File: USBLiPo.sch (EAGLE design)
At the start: 11 parts, among them IC1 LTC4054, J1 Battery, J2 USB, Q1 2N7002

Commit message: fixed charge current program
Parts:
- Q1: device freetronics-master-v1:MOSFET-NCHANNELSMD -> freetronics-luke:2N7002
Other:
- moved on the sheet: Q1
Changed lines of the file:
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@@
 <part name="IC1" library="freetronics-luke" deviceset="LTC4054" device=""/>
 <part name="U$1" library="freetronics-luke" deviceset="GND" device=""/>
-<part name="Q1" library="freetronics-master-v1" deviceset="MOSFET-NCHANNEL" device="SMD" value="2N7002"/>
 <part name="R1" library="freetronics" deviceset="RESISTOR" device="0603" value="1k"/>
 <part name="R2" library="freetronics" deviceset="RESISTOR" device="0603" value="10k"/>
@@
 <part name="LED2" library="freetronics-master-v1" deviceset="LED" device="0603" value="Red"/>
 <part name="J2" library="freetronics-luke" deviceset="USB-FT" device="" value="USB"/>
+<part name="Q1" library="freetronics-luke" deviceset="2N7002" device=""/>
 </parts>
 <sheets>
@@
 </instance>
 <instance part="U$1" gate="G$1" x="86.36" y="53.34"/>
-<instance part="Q1" gate="G$1" x="132.08" y="68.58" smashed="yes">
-<attribute name="NAME" x="119.38" y="73.66" size="1.27" layer="95"/>
-<attribute name="VALUE" x="119.38" y="71.12" size="1.27" layer="96"/>
-</instance>
 <instance part="R1" gate="G$1" x="109.22" y="91.44" smashed="yes" rot="MR180">
 <attribute name="NAME" x="106.68" y="96.52" size="1.27" layer="95"/>
@@
 </instance>
 <instance part="J2" gate="G$1" x="35.56" y="71.12"/>
+<instance part="Q1" gate="G$1" x="132.08" y="68.58" smashed="yes">
+<attribute name="NAME" x="119.38" y="73.66" size="1.27" layer="95"/>
+<attribute name="VALUE" x="119.38" y="71.12" size="1.27" layer="96"/>
+</instance>
 </instances>
 <busses>
@@
 <segment>
 <wire x1="132.08" y1="63.5" x2="132.08" y2="55.88" width="0.1524" layer="91"/>
+<pinref part="U$6" gate="G$1" pin="GND"/>
 <pinref part="Q1" gate="G$1" pin="S"/>
-<pinref part="U$6" gate="G$1" pin="GND"/>
 </segment>
 <segment>
@@
 <segment>
 <wire x1="132.08" y1="78.74" x2="132.08" y2="73.66" width="0.1524" layer="91"/>
+<pinref part="LED2" gate="G$1" pin="C"/>
 <pinref part="Q1" gate="G$1" pin="D"/>
-<pinref part="LED2" gate="G$1" pin="C"/>
 </segment>
 </net>
@@
 <net name="N$6" class="0">
 <segment>
-<wire x1="124.46" y1="68.58" x2="116.84" y2="68.58" width="0.1524" layer="91"/>
+<wire x1="127" y1="68.58" x2="116.84" y2="68.58" width="0.1524" layer="91"/>
 <wire x1="116.84" y1="68.58" x2="104.14" y2="68.58" width="0.1524" layer="91"/>
 <wire x1="101.6" y1="78.74" x2="101.6" y2="71.12" width="0.1524" layer="91"/>
@@
 <junction x="116.84" y="68.58"/>
 <pinref part="IC1" gate="G$1" pin="!CHRG"/>
-<pinref part="Q1" gate="G$1" pin="G"/>
 <pinref part="R2" gate="G$1" pin="2"/>
 <pinref part="LED1" gate="G$1" pin="C"/>
-</segment>
-</net>
+<pinref part="Q1" gate="G$1" pin="G"/>
+</segment>
+</net>

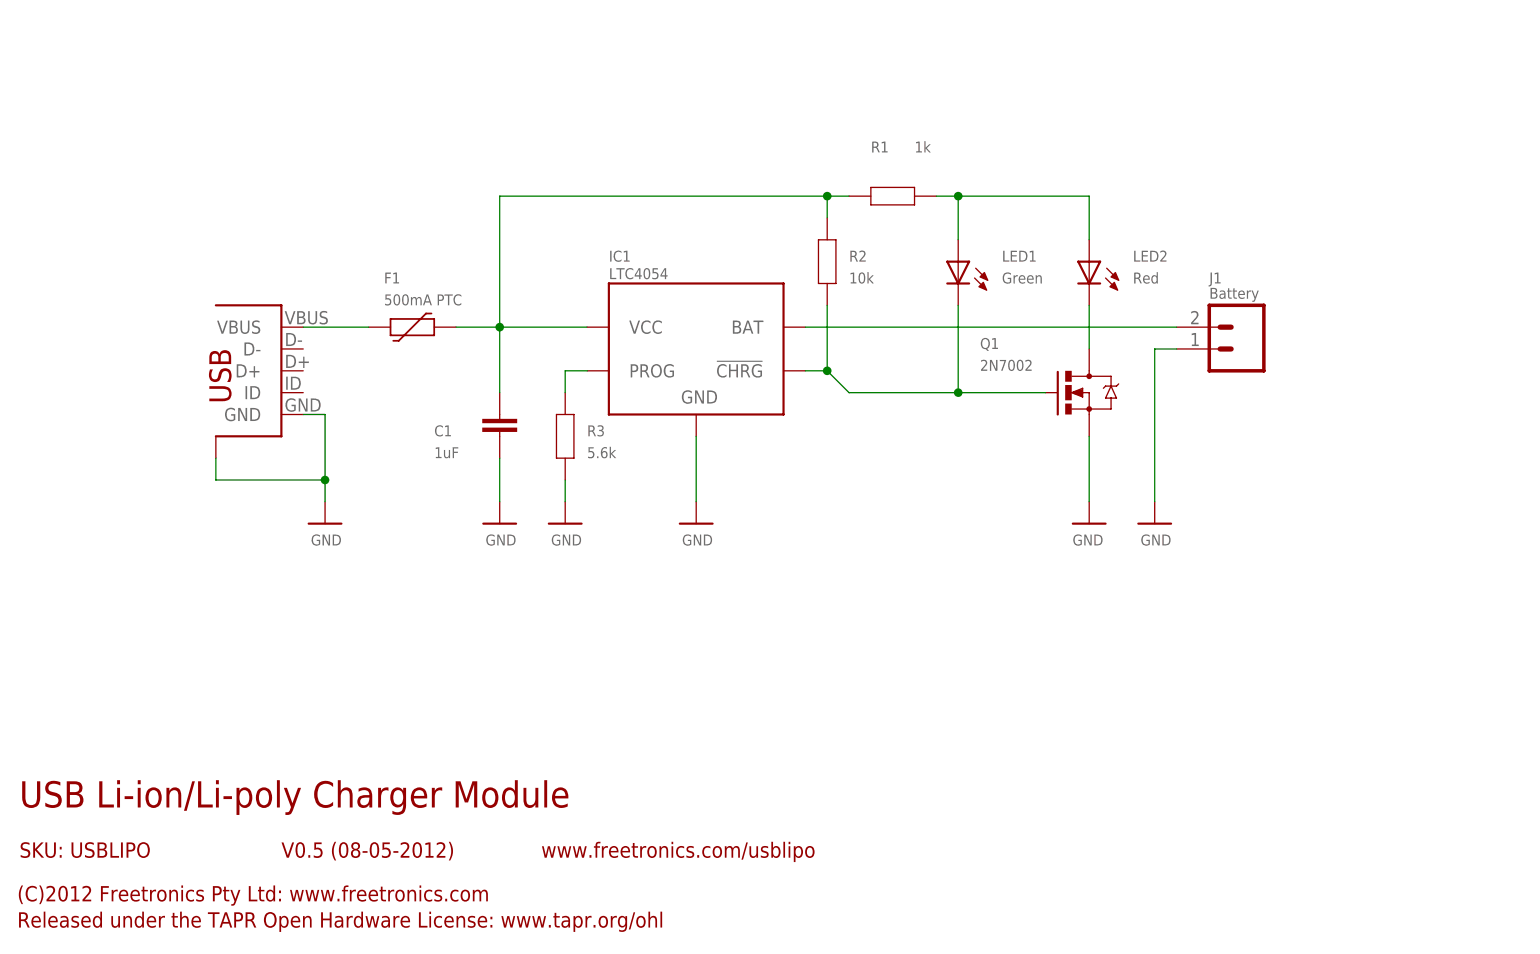
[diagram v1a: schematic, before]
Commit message: changed JST connector to through-hole right angle
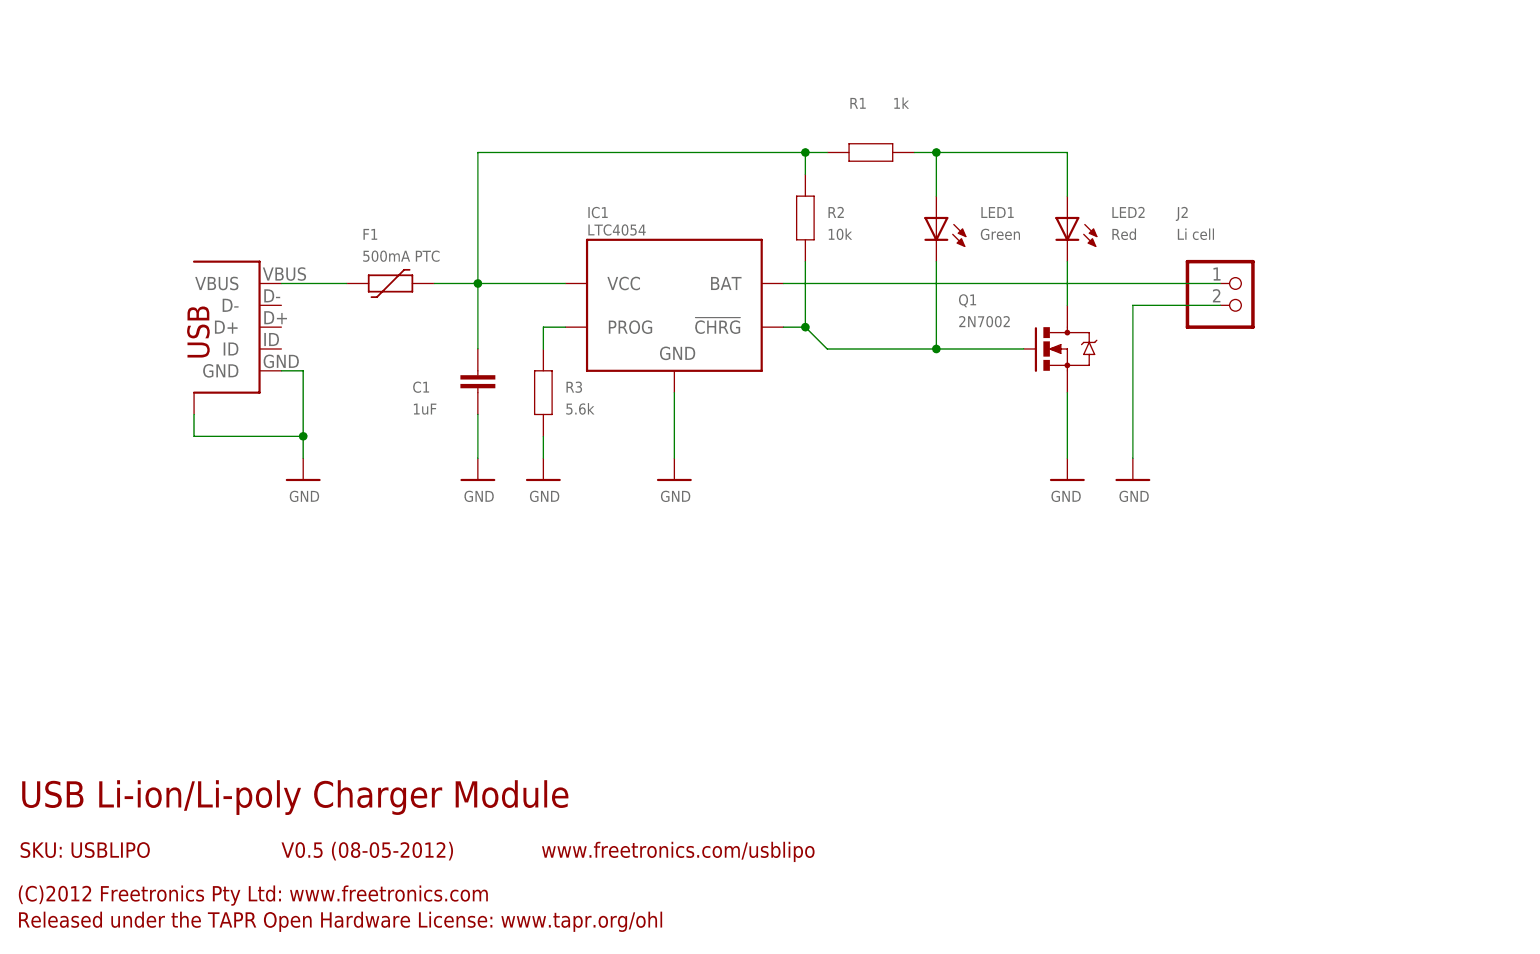
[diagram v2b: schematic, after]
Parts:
- J1: value Battery -> USB; device freetronics-master-v1:M02-JST-2MM-SMT -> freetronics-luke:USB-FT
- J2: value USB -> Li cell; device freetronics-luke:USB-FT -> adafruit:JST_2PIN-THM-RA
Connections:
- net GND: now also J1.GND, J1.SH$1, J2.1; no longer J1.1, J2.GND, J2.SH$1
- net N$113: now also J1.VBUS; no longer J2.VBUS
- net N$4: now also J2.2; no longer J1.2
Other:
- moved on the sheet: C1, F1, IC1, LED1, LED2, Q1, R1, R2, R3

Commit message: foo
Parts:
- removed J2: Li cell, adafruit:JST_2PIN-THM-RA
- added B1: LiPo cell, freetronics-luke:2P-JST-TH-RA
- added R4, R5: 10k, freetronics:RESISTOR0603
- added S1, S2: SJ, freetronics-luke:SJ
- LED1: value Green -> Charge
- LED2: value Red -> Standby
- R3: value 5.6k -> 3k3
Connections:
- new net N$5: R3.1, S1.1
- new net N$7: R4.1, S2.1
- net GND: now also B1.-, R4.2, R5.2; no longer J2.1
- net N$3: now also R5.1, S1.2, S2.2; no longer R3.1
- net N$4: now also B1.+; no longer J2.2
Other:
- note added: "0 0 100 mA"
- note added: "0 1 200 mA"
- note added: "1 0 403 mA"
- note added: "1 1 503 mA"
- note added: "2-pin 2.0mm JST"
- note added: "Green"
- note added: "S1 S2 Charge current"
- note added: "USER MUST ALWAYS DOUBLE CHECK BATTERY POLARITY BEFORE USE BECAUSE SOME LIPO CELLS ARE NOT STANDARD."
- note added: "Yellow"
- note removed: "2-pin SMD JST"
- note removed: "Iprog = 1000 V / 5600 ohms = 179 mA (Just a little under 0.2C for a typical 1.0 Ah LiPo cell.)"
- note removed: "JST CONNECTOR ORIENTATION/POLARITY MUST BE CHECKED. ARE ALL LIPO CELLS ``STANDARD''?"
- note removed: "Mates with LiPo cell."
- note removed: "Same as SparkFun one."
- note removed: "The FET allows two LEDs to be driven"
- note removed: "To do: Documentation of LED truth table, charging states."
- note removed: "USB shield connected to ground. Not completely sure if this is best."
- note removed: "from the LTC4054's open-drain output."
- moved on the sheet: C1, F1, LED1, LED2, Q1, R1, R2, R3

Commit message: foo
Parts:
- R1: value 1k -> 10k
- R2: value 10k -> 1k
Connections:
- net N$6: now also R1.2; no longer R2.2
- net N$8: now also R2.2; no longer R1.2
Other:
- moved on the sheet: R1, R2
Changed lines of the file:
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@@
 <part name="IC1" library="freetronics-luke" deviceset="LTC4054" device=""/>
 <part name="U$1" library="freetronics-luke" deviceset="GND" device=""/>
-<part name="R1" library="freetronics" deviceset="RESISTOR" device="0603" value="1k"/>
-<part name="R2" library="freetronics" deviceset="RESISTOR" device="0603" value="10k"/>
+<part name="R2" library="freetronics" deviceset="RESISTOR" device="0603" value="1k"/>
+<part name="R1" library="freetronics" deviceset="RESISTOR" device="0603" value="10k"/>
 <part name="C1" library="freetronics" deviceset="CAP" device="0603" value="1uF"/>
 <part name="U$4" library="freetronics-luke" deviceset="GND" device=""/>
@@
 </instance>
 <instance part="U$1" gate="G$1" x="106.68" y="50.8"/>
-<instance part="R1" gate="G$1" x="132.08" y="104.14" smashed="yes" rot="MR270">
+<instance part="R2" gate="G$1" x="132.08" y="104.14" smashed="yes" rot="MR270">
 <attribute name="NAME" x="134.62" y="106.68" size="1.27" layer="95"/>
 <attribute name="VALUE" x="134.62" y="104.14" size="1.27" layer="96"/>
 </instance>
-<instance part="R2" gate="G$1" x="121.92" y="104.14" smashed="yes" rot="MR270">
+<instance part="R1" gate="G$1" x="121.92" y="104.14" smashed="yes" rot="MR270">
 <attribute name="NAME" x="124.46" y="106.68" size="1.27" layer="95"/>
 <attribute name="VALUE" x="124.46" y="104.14" size="1.27" layer="96"/>
@@
 <pinref part="LED1" gate="G$1" pin="A"/>
 <pinref part="LED2" gate="G$1" pin="A"/>
-<pinref part="R1" gate="G$1" pin="2"/>
+<pinref part="R2" gate="G$1" pin="2"/>
 <wire x1="132.08" y1="99.06" x2="132.08" y2="96.52" width="0.1524" layer="91"/>
 <junction x="132.08" y="96.52"/>
@@
 <junction x="63.5" y="81.28"/>
 <junction x="121.92" y="111.76"/>
+<pinref part="R2" gate="G$1" pin="1"/>
 <pinref part="R1" gate="G$1" pin="1"/>
-<pinref part="R2" gate="G$1" pin="1"/>
 <pinref part="F1" gate="G$1" pin="P$2"/>
 <pinref part="IC1" gate="G$1" pin="VCC"/>
@@
 <junction x="132.08" y="76.2"/>
 <pinref part="IC1" gate="G$1" pin="!CHRG"/>
-<pinref part="R2" gate="G$1" pin="2"/>
+<pinref part="R1" gate="G$1" pin="2"/>
 <pinref part="LED1" gate="G$1" pin="C"/>
 <pinref part="Q1" gate="G$1" pin="G"/>

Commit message: foo
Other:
- note added: "2.0mm JST"
- note removed: "2-pin 2.0mm JST"
- moved on the sheet: LED2, Q1
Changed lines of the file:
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@@
 <setting verticaltext="up"/>
 </settings>
-<grid distance="0.1" unitdist="inch" unit="inch" style="lines" multiple="1" display="yes" altdistance="0.01" altunitdist="inch" altunit="inch"/>
+<grid distance="0.1" unitdist="inch" unit="inch" style="lines" multiple="1" display="no" altdistance="0.01" altunitdist="inch" altunit="inch"/>
 <layers>
 <layer number="1" name="Top" color="4" fill="1" visible="no" active="no"/>
@@
 <text x="53.34" y="86.36" size="1.27" layer="98">1812</text>
 <text x="55.88" y="55.88" size="1.27" layer="98">0603</text>
-<text x="129.54" y="58.42" size="1.27" layer="98">2-pin 2.0mm JST</text>
-<text x="134.62" y="68.58" size="1.27" layer="98">SOT-23</text>
+<text x="129.54" y="58.42" size="1.27" layer="98">2.0mm JST</text>
+<text x="154.94" y="68.58" size="1.27" layer="98">SOT-23</text>
 <text x="124.46" y="101.6" size="1.27" layer="98">0603</text>
 <text x="137.16" y="86.36" size="1.27" layer="98">0603</text>
-<text x="152.4" y="86.36" size="1.27" layer="98">0603</text>
+<text x="154.94" y="86.36" size="1.27" layer="98">0603</text>
 <text x="134.62" y="101.6" size="1.27" layer="98">0603</text>
 <text x="93.98" y="55.88" size="1.27" layer="98">0603</text>
@@
 <wire x1="134.62" y1="10.16" x2="134.62" y2="38.1" width="0.1524" layer="98"/>
 <text x="137.16" y="83.82" size="1.27" layer="98">Green</text>
-<text x="152.4" y="83.82" size="1.27" layer="98">Yellow</text>
+<text x="154.94" y="83.82" size="1.27" layer="98">Yellow</text>
+<wire x1="121.92" y1="73.66" x2="142.24" y2="73.66" width="0.3048" layer="98" style="shortdash"/>
+<wire x1="142.24" y1="73.66" x2="142.24" y2="55.88" width="0.3048" layer="98" style="shortdash"/>
+<wire x1="142.24" y1="55.88" x2="121.92" y2="55.88" width="0.3048" layer="98" style="shortdash"/>
+<wire x1="121.92" y1="55.88" x2="121.92" y2="73.66" width="0.3048" layer="98" style="shortdash"/>
 </plain>
 <instances>
@@
 </instance>
 <instance part="U$4" gate="G$1" x="63.5" y="50.8"/>
-<instance part="U$6" gate="G$1" x="147.32" y="50.8" rot="MR0"/>
+<instance part="U$6" gate="G$1" x="149.86" y="50.8" rot="MR0"/>
 <instance part="U$7" gate="G$1" x="127" y="50.8"/>
 <instance part="F1" gate="G$1" x="53.34" y="81.28" smashed="yes">
@@
 <attribute name="VALUE" x="137.16" y="88.9" size="1.27" layer="96"/>
 </instance>
-<instance part="LED2" gate="G$1" x="147.32" y="91.44" smashed="yes" rot="MR0">
-<attribute name="NAME" x="152.4" y="91.44" size="1.27" layer="95"/>
-<attribute name="VALUE" x="152.4" y="88.9" size="1.27" layer="96"/>
+<instance part="LED2" gate="G$1" x="149.86" y="91.44" smashed="yes" rot="MR0">
+<attribute name="NAME" x="154.94" y="91.44" size="1.27" layer="95"/>
+<attribute name="VALUE" x="154.94" y="88.9" size="1.27" layer="96"/>
 </instance>
 <instance part="J1" gate="G$1" x="35.56" y="76.2"/>
-<instance part="Q1" gate="G$1" x="147.32" y="76.2" smashed="yes">
-<attribute name="NAME" x="134.62" y="73.66" size="1.27" layer="95"/>
-<attribute name="VALUE" x="134.62" y="71.12" size="1.27" layer="96"/>
+<instance part="Q1" gate="G$1" x="149.86" y="76.2" smashed="yes">
+<attribute name="NAME" x="154.94" y="73.66" size="1.27" layer="95"/>
+<attribute name="VALUE" x="154.94" y="71.12" size="1.27" layer="96"/>
 </instance>
 <instance part="R3" gate="G$1" x="71.12" y="60.96" smashed="yes" rot="MR270">
@@
 </segment>
 <segment>
-<wire x1="147.32" y1="71.12" x2="147.32" y2="53.34" width="0.1524" layer="91"/>
+<wire x1="149.86" y1="71.12" x2="149.86" y2="53.34" width="0.1524" layer="91"/>
 <pinref part="U$6" gate="G$1" pin="GND"/>
 <pinref part="Q1" gate="G$1" pin="S"/>
@@
 <net name="N$1" class="0">
 <segment>
-<wire x1="147.32" y1="86.36" x2="147.32" y2="81.28" width="0.1524" layer="91"/>
+<wire x1="149.86" y1="86.36" x2="149.86" y2="81.28" width="0.1524" layer="91"/>
 <pinref part="LED2" gate="G$1" pin="C"/>
 <pinref part="Q1" gate="G$1" pin="D"/>
@@
 <net name="N$8" class="0">
 <segment>
-<wire x1="132.08" y1="96.52" x2="147.32" y2="96.52" width="0.1524" layer="91"/>
-<wire x1="147.32" y1="96.52" x2="147.32" y2="93.98" width="0.1524" layer="91"/>
+<wire x1="132.08" y1="96.52" x2="149.86" y2="96.52" width="0.1524" layer="91"/>
+<wire x1="149.86" y1="96.52" x2="149.86" y2="93.98" width="0.1524" layer="91"/>
 <wire x1="132.08" y1="93.98" x2="132.08" y2="96.52" width="0.1524" layer="91"/>
 <pinref part="LED1" gate="G$1" pin="A"/>
@@
 <net name="N$6" class="0">
 <segment>
-<wire x1="142.24" y1="76.2" x2="132.08" y2="76.2" width="0.1524" layer="91"/>
+<wire x1="144.78" y1="76.2" x2="132.08" y2="76.2" width="0.1524" layer="91"/>
 <wire x1="132.08" y1="76.2" x2="121.92" y2="76.2" width="0.1524" layer="91"/>
 <wire x1="121.92" y1="99.06" x2="121.92" y2="76.2" width="0.1524" layer="91"/>
